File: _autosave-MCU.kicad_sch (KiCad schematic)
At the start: 106 parts, among them J1 FTDI, J10 mist, J12 Water_Level, J13 Main_Input_Jack, J14 Battery, J15 Display, J16 Rotary encoder, J17 Temp, J18 Temp2, J19 Water_Pump, J2 LED, J20 Conn_01x04_Socket, J3 C8465, J4 C8465, J6 C8465, J8 Fan_Exhaust, J9 Fan_Continous, K1 G5NB-1A-E DC12, Q10 AO3406, Q2 AO3406, Q3 AO3406, Q4 AO3406, Q5 AO3406, Q6 AO3406, Q7 SI2301, Q8 AO3406, Q9 AO3406, SW1 SW_Omron_B3FS, SW2 SW_Omron_B3FS, U1 TPS63070RNMR, U2 ESP32-WROOM-32, U3 AMS1117-5.0, U5 PCF8574, U6 MAX17048G_T10, U7 TP4056, U8 DS1307+, U9 G5NB-1A-E DC12, Y1 32.768kHz Quartz Crystal

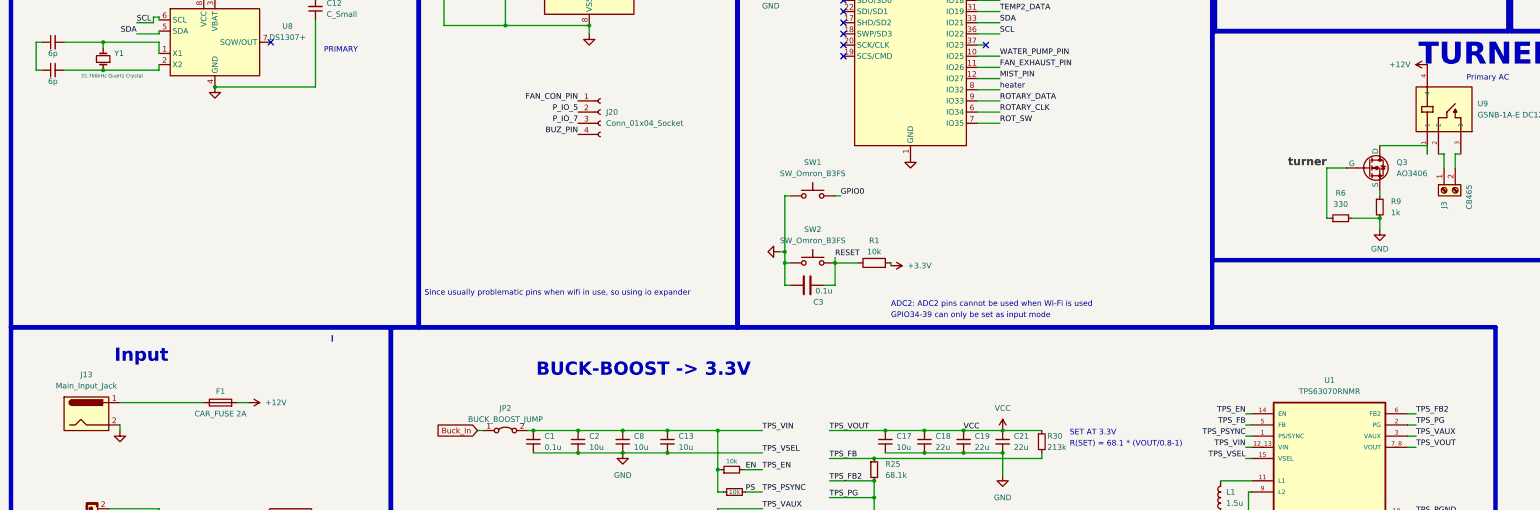
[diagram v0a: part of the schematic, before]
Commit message: changed picture in readme
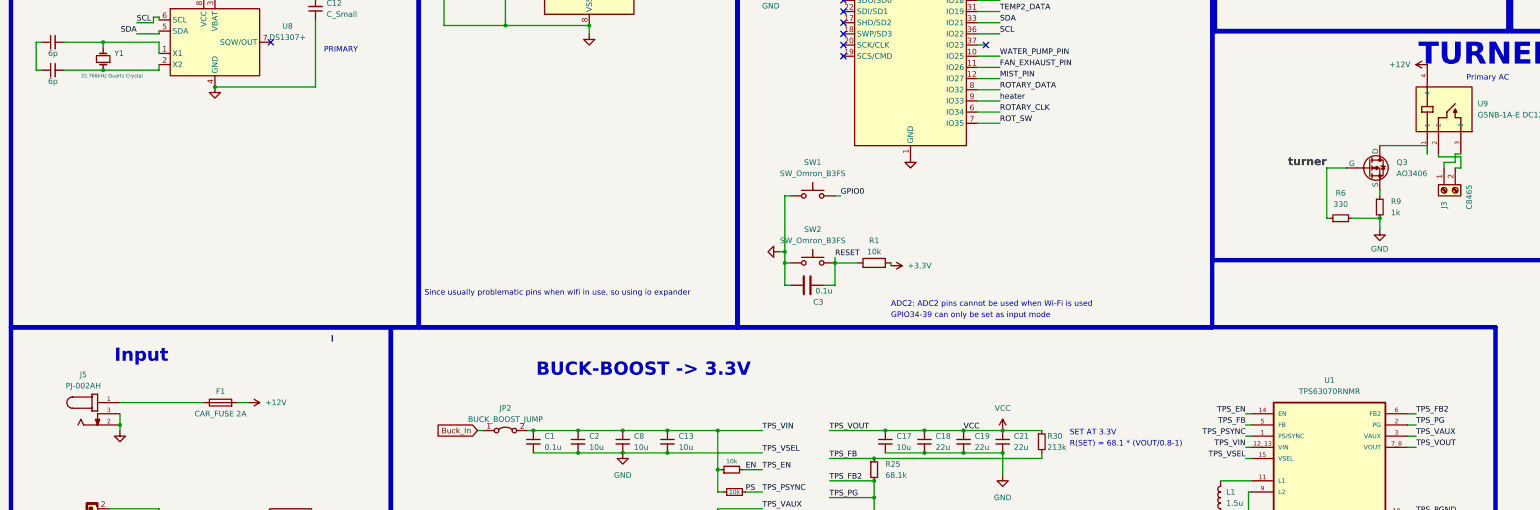
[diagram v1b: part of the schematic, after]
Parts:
- removed J13: Main_Input_Jack, Connector_BarrelJack:BarrelJack_CLIFF_FC681465S_SMT_Horizontal, symbol Connector:Jack-DC
- removed J20: Conn_01x04_Socket, Connector_JST:JST_GH_SM04B-GHS-TB_1x04-1MP_P1.25mm_Horizontal, symbol Connector:Conn_01x04_Socket
- added J5: PJ-002AH, PJ-002AH:CUI_PJ-002AH, symbol dc-jack:PJ-002AH
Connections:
- net GND: now also J5.2, J5.3
- net ROTARY_DATA: now also U2.8 (IO32); no longer U2.9 (IO33)
- net heater: now also U2.9 (IO33); no longer U2.8 (IO32)
- net at F1.1: now also J5.1
- net at J3.1 (Pin_1): now also U9.3; no longer U9.2
- net at J3.2 (Pin_2): now also U9.2; no longer U9.3
